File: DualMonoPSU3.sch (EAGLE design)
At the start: 19 parts, among them J1 1935161

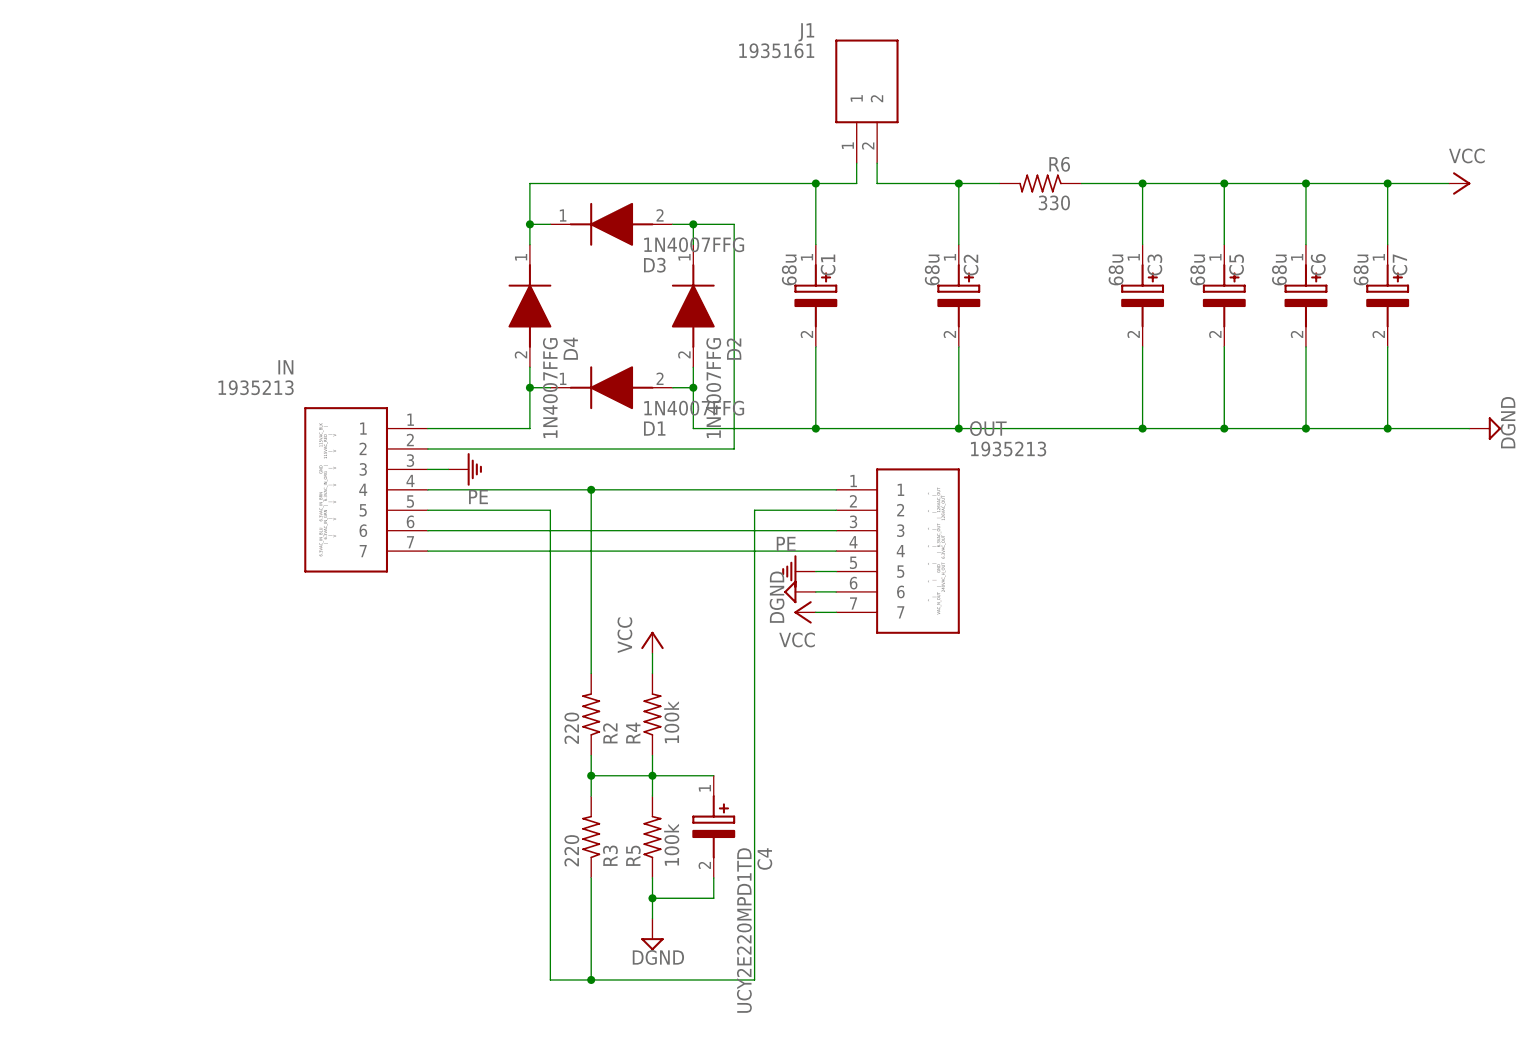
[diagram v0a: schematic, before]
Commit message: submitted PSU board for fabrication
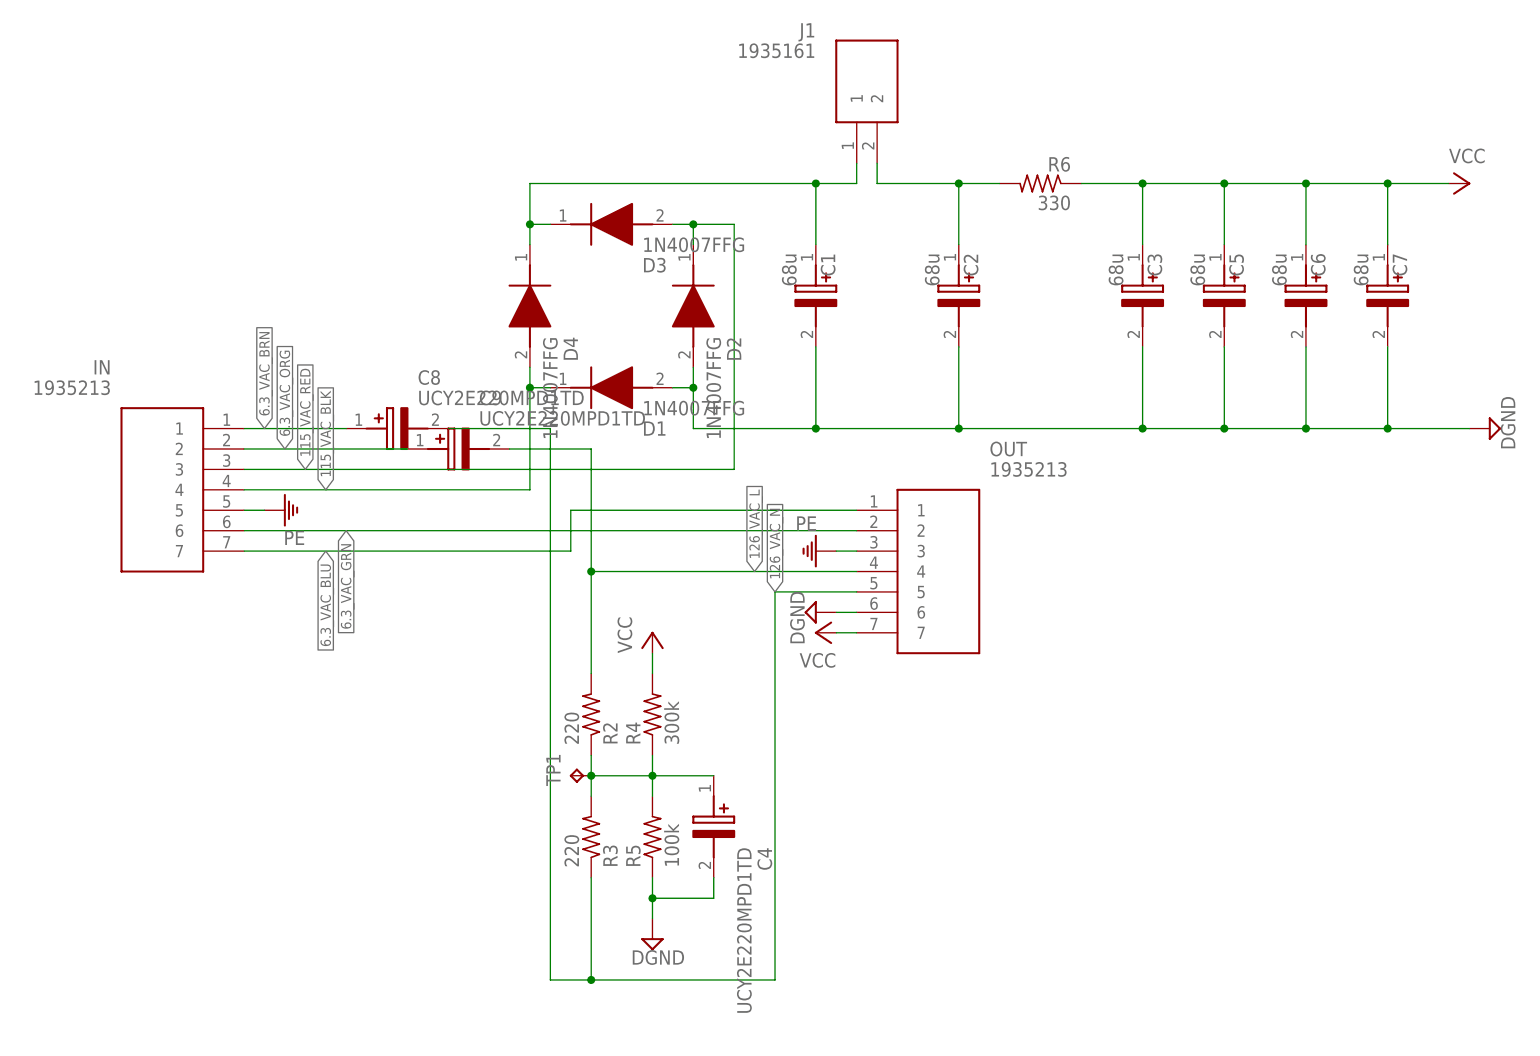
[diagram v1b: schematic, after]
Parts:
- added C8, C9: UCY2E220MPD1TD, UCY2E220MPD1TD:UCY2E220MPD1TD
- added TP1: TPB2,54, testpad:TPB2,54
- R4: value 100k -> 300k
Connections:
- removed net N$1: IN.5, OUT.2, R3.1
- removed net N$2: D1.K, D4.A, IN.1
- removed net N$4: D2.K, D3.A, IN.2
- removed net N$7: IN.4, OUT.1, R2.2
- removed net N$8: IN.6, OUT.3
- removed net N$9: IN.7, OUT.4
- new net 115_VAC_BLK: D1.K, D4.A, IN.4
- new net 115_VAC_RED: D2.K, D3.A, IN.3
- new net 126_VAC_L: C9.-, OUT.4, R2.2
- new net 126_VAC_N: C8.-, OUT.5, R3.1
- new net 6.3_VAC_BLU: IN.7, OUT.1
- new net 6.3_VAC_BRN: C8.+, IN.1
- new net 6.3_VAC_GRN: IN.6, OUT.2
- new net 6.3_VAC_ORG: C9.+, IN.2
- net N$6: now also TP1.TP
- net PE: now also IN.5, OUT.3; no longer IN.3, OUT.5
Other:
- note removed: "6.3VAC_IN_BLU 6.3VAC_IN_BRN GND 115VAC_BLK | 6.3VAC_IN_GRN | 6.3VAC_IN_ORG | 115VAC_RED | | | | | | | | V V V V V V V"
- note removed: "^ ^ ^ ^ ^ ^ ^ | | | | | | | VAC_N_OUT | GND | 6.3VAC_OUT | 126VAC_OUT 240VAC_H_OUT 6.3VAC_OUT 126VAC_OUT"
- moved on the sheet: IN, OUT

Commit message: Combi progress
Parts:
- renumbered C1 to C1P, C2 to C2P, C3 to C3P, C4 to C4P, C5 to C5P, C6 to C6P, C7 to C7P, C8 to C8P, C9 to C9P, R2 to R2P, R3 to R3P, R4 to R4P, R5 to R5P, R6 to R6P
